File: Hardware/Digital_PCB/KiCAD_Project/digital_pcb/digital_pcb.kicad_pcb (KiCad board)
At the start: 4 copper layers, 75 x 84.8 mm, 85 parts, among them J1 ISP, J2 Board to Board, J3 Conn_01x02, J4 Spare 1, J5 Power, J6 Power Switch, J7 Conn_01x02, Q1 MMBT3904, U1 STM32F103CBTx, U10 TPS793, U2 BNO055, U3 HTU21D, U4 ADS1220, U5 KC2520B-C2, U6 SN74LVC1G17-EP, U7 LT1521-3.3, U8 TEC 2-0921, U9 TPS723, Y1 8MHz, Y2 32.768kHz

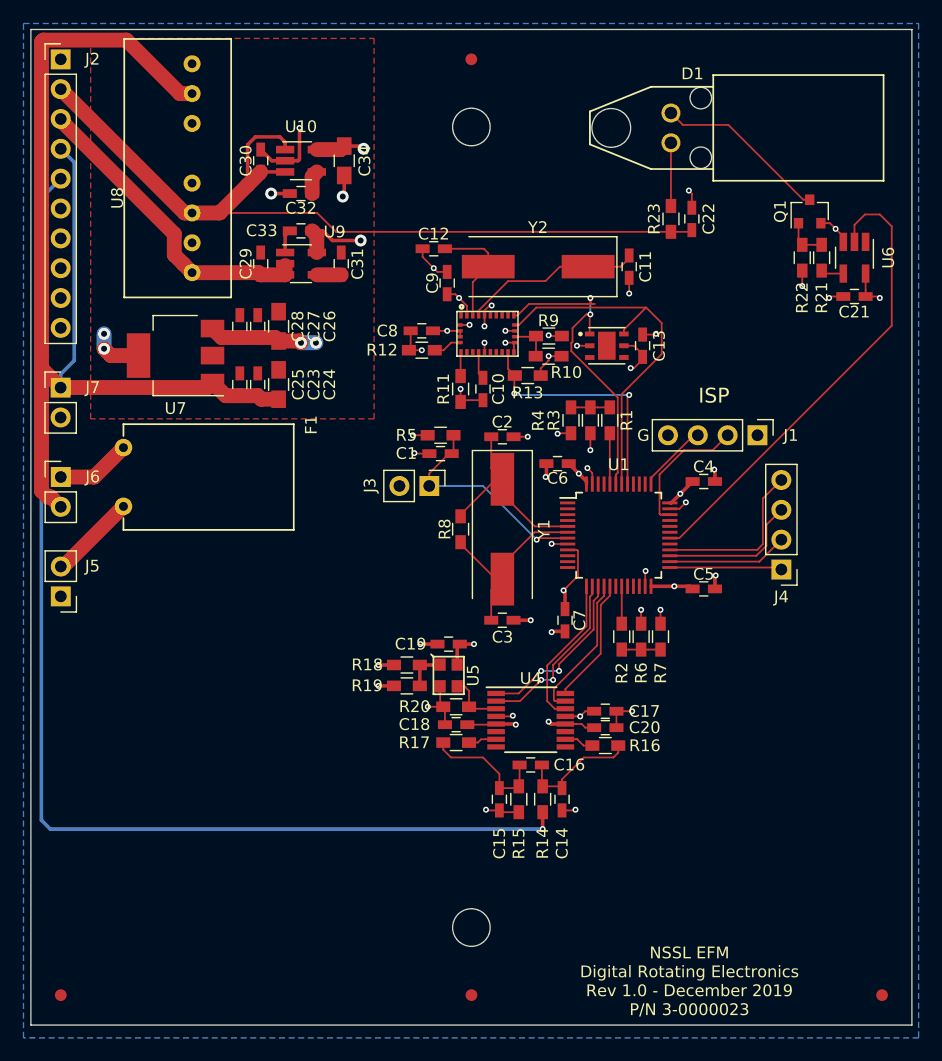
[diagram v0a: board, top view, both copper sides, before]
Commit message: Add pullups and divider for ADC input.
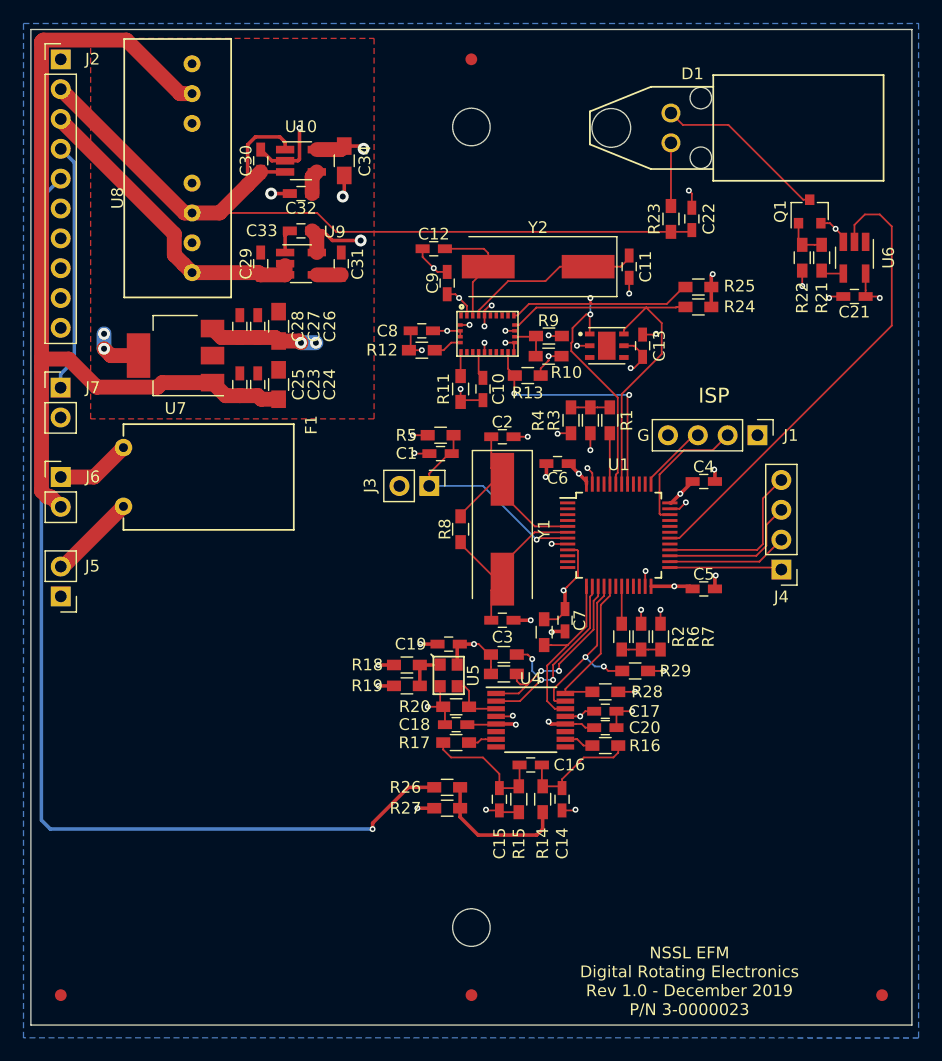
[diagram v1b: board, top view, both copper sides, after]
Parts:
- added R24: 10k, Resistors_SMD:R_0603_HandSoldering, F.Cu at (173.0, 77.5)
- added R25: 10k, Resistors_SMD:R_0603_HandSoldering, F.Cu at (173.0, 75.8)
- added R26: 10k, Resistors_SMD:R_0603_HandSoldering, F.Cu at (151.6, 118.4)
- added R27: 10k, Resistors_SMD:R_0603_HandSoldering, F.Cu at (151.6, 120.1)
- added R28: 10k, Resistors_SMD:R_0603_HandSoldering, F.Cu at (165.1, 110.2)
- added R29: 10k, Resistors_SMD:R_0603_HandSoldering, F.Cu at (167.6, 108.5)
- added R30: 10k, Resistors_SMD:R_0603_HandSoldering, F.Cu at (156.5, 108.7)
- added R31: 10k, Resistors_SMD:R_0603_HandSoldering, F.Cu at (156.5, 107.1)
- added R32: 10k, Resistors_SMD:R_0603_HandSoldering, F.Cu at (159.9, 105.2)
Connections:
- R14 pad 2: AMP_OUT -> Net-(R14-Pad2)
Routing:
- net Net-(R14-Pad2): track 0.00 -> 11.8 mm
- net +3V3: track 51.3 -> 62.6 mm, vias 17 -> 20
- net AMP_OUT: track 99.7 -> 90.8 mm
- net I2C_SDA: track 28.0 -> 36.3 mm
- net SPI1_MISO: track 12.5 -> 16.1 mm, vias 0 -> 2
- net ADC_CS: track 15.0 -> 18.5 mm, vias 2 -> 3
- net I2C_SCL: track 31.8 -> 35.2 mm
- net SPI1_MOSI: track 10.7 -> 13.1 mm
- net ADC_~DRDY: track 13.0 -> 15.0 mm
- net SPI1_SCLK: track 14.7 -> 16.4 mm
- net GND: track 75.8 -> 77.3 mm, vias 42 -> 43
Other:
- board text added: "AMP OUT"

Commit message: Digital PCB Rev 1.0 complete.
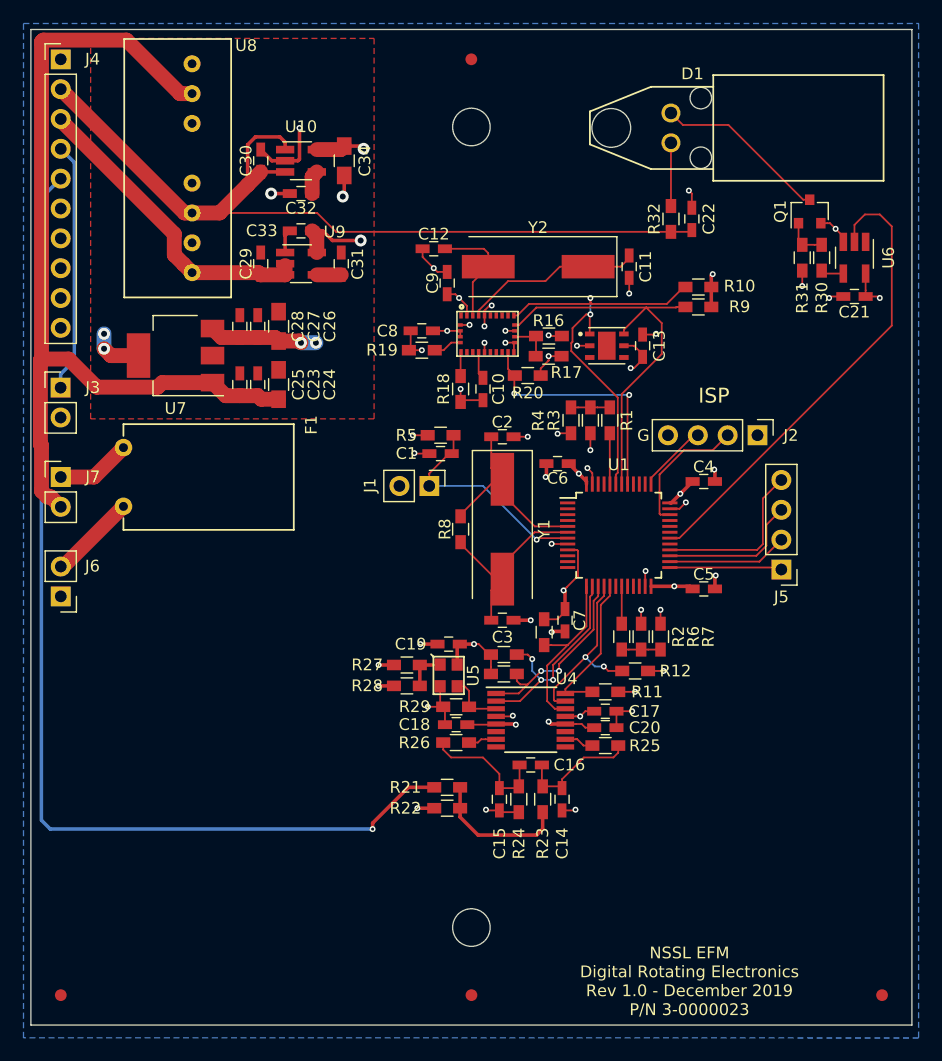
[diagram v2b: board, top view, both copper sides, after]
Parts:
- renumbered J3 to J1, J1 to J2, J7 to J3, J2 to J4, J4 to J5, J5 to J6, J6 to J7, R25 to R10, R28 to R11, R29 to R12, R30 to R13, R31 to R14, R32 to R15, R9 to R16, R10 to R17, R11 to R18, R12 to R19, R13 to R20, R26 to R21, R27 to R22, R14 to R23, R15 to R24, R16 to R25, R17 to R26, R18 to R27, R19 to R28, R20 to R29, R21 to R30, R22 to R31, R23 to R32, R24 to R9

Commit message: Fix flipped fiber transmtter footprint, closes #4.
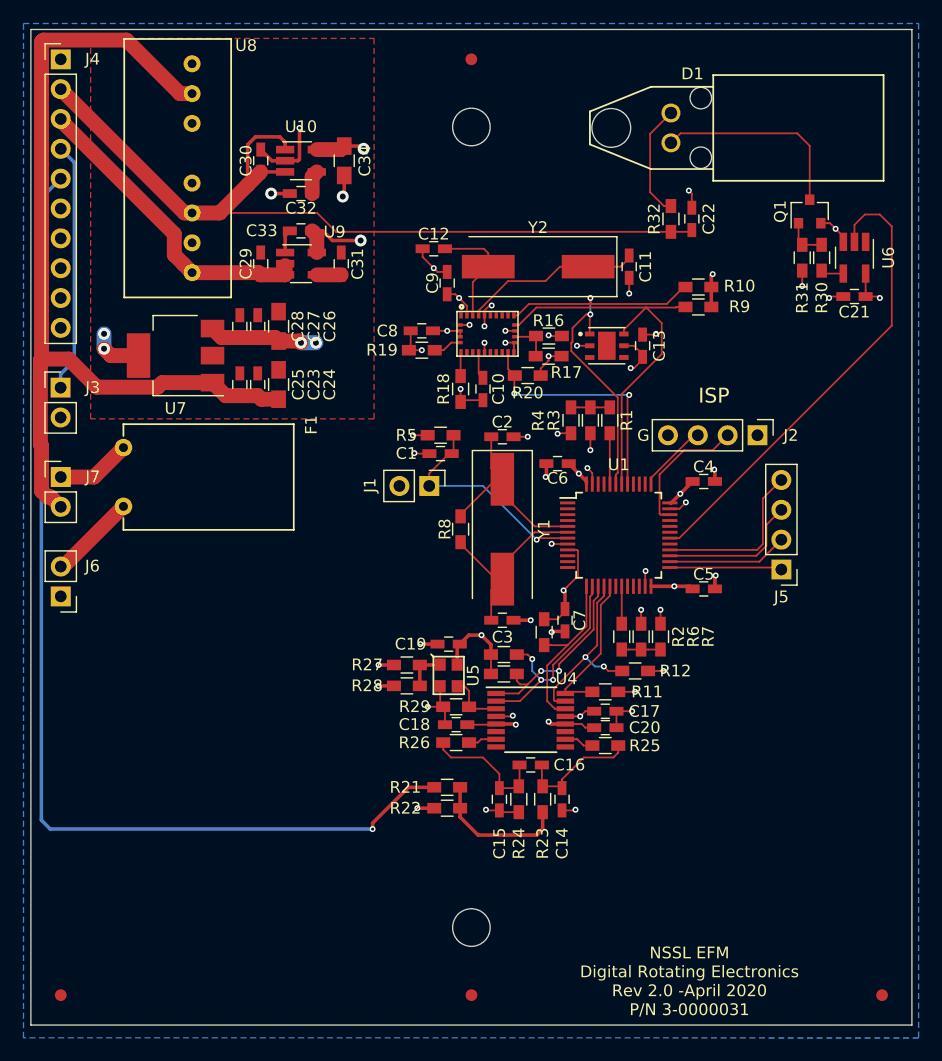
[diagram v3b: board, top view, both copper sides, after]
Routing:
- net Net-(D1-Pad2): track 5.38 -> 9.74 mm
- net Net-(D1-Pad1): track 14.9 -> 17.2 mm
- net +3V3: track 62.6 -> 63.7 mm
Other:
- board text added: "NSSL EFM Digital Rotating Electronics Rev 2.0 -April 2020 P/N 3-0000031"
- board text removed: "NSSL EFM Digital Rotating Electronics Rev 1.0 - December 2019 P/N 3-0000023"

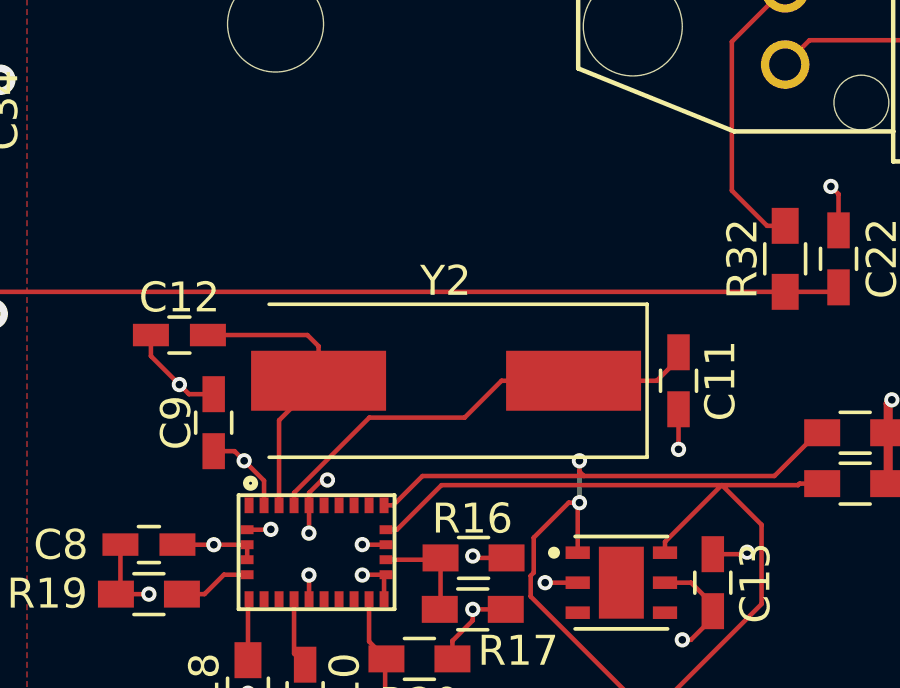
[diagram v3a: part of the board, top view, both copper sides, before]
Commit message: Update IMU crystal footprint to 4-SOJ. closes #5.
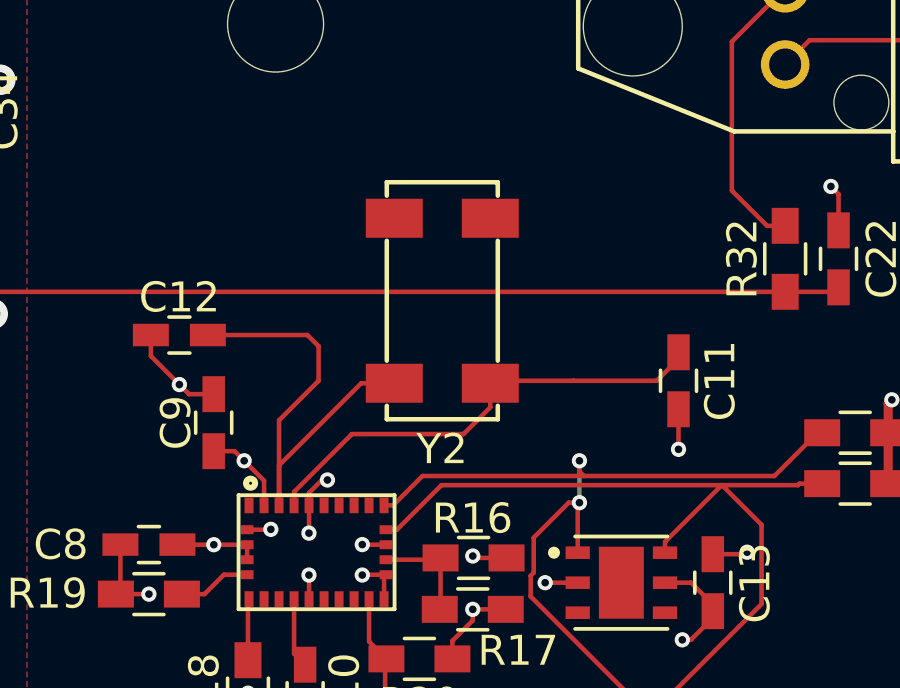
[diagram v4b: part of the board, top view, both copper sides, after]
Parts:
- Y2: footprint Crystals:Crystal_SMD_HC49-SD -> lib_fp:4-SOJ
- moved Y2 2.67 mm to (159.3, 71.4), turned to 90 degrees
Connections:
- J4 pad 10: (no net) -> Net-(J4-Pad10)
- J4 pad 7: (no net) -> Net-(J4-Pad7)
- J4 pad 8: (no net) -> Net-(J4-Pad8)
- J4 pad 9: (no net) -> Net-(J4-Pad9)
- U1 pad 1: (no net) -> Net-(U1-Pad1)
- U1 pad 10: (no net) -> Net-(U1-Pad10)
- U1 pad 11: (no net) -> Net-(U1-Pad11)
- U1 pad 12: (no net) -> Net-(U1-Pad12)
- U1 pad 18: (no net) -> Net-(U1-Pad18)
- U1 pad 2: (no net) -> Net-(U1-Pad2)
- U1 pad 20: (no net) -> Net-(U1-Pad20)
- U1 pad 21: (no net) -> Net-(U1-Pad21)
- U1 pad 22: (no net) -> Net-(U1-Pad22)
- U1 pad 29: (no net) -> Net-(U1-Pad29)
- U1 pad 3: (no net) -> Net-(U1-Pad3)
- U1 pad 31: (no net) -> UART1_RX
- U1 pad 32: (no net) -> Net-(U1-Pad32)
- U1 pad 33: (no net) -> Net-(U1-Pad33)
- U1 pad 38: (no net) -> Net-(U1-Pad38)
- U1 pad 39: (no net) -> Net-(U1-Pad39)
- U1 pad 4: (no net) -> Net-(U1-Pad4)
- U1 pad 40: (no net) -> Net-(U1-Pad40)
- U1 pad 45: (no net) -> Net-(U1-Pad45)
- U1 pad 46: (no net) -> Net-(U1-Pad46)
- U2 pad 1: (no net) -> Net-(U2-Pad1)
- U2 pad 11: (no net) -> Net-(U2-Pad11)
- U2 pad 12: (no net) -> Net-(U2-Pad12)
- U2 pad 13: (no net) -> Net-(U2-Pad13)
- U2 pad 21: (no net) -> Net-(U2-Pad21)
- U2 pad 22: (no net) -> Net-(U2-Pad22)
- U2 pad 23: (no net) -> Net-(U2-Pad23)
- U2 pad 24: (no net) -> Net-(U2-Pad24)
- U2 pad 7: (no net) -> Net-(U2-Pad7)
- U2 pad 8: (no net) -> Net-(U2-Pad8)
- U3 pad 3: (no net) -> Net-(U3-Pad3)
- U3 pad 4: (no net) -> Net-(U3-Pad4)
- U3 pad 7: (no net) -> Net-(U3-Pad7)
- U4 pad 11: (no net) -> Net-(U4-Pad11)
- U4 pad 6: (no net) -> Net-(U4-Pad6)
- U4 pad 8: (no net) -> Net-(U4-Pad8)
- U4 pad 9: (no net) -> Net-(U4-Pad9)
- U6 pad 1: (no net) -> Net-(U6-Pad1)
- U8 pad 3: (no net) -> Net-(U8-Pad3)
- U8 pad 5: (no net) -> Net-(U8-Pad5)
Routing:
- net Net-(C12-Pad2): track 9.69 -> 16.0 mm

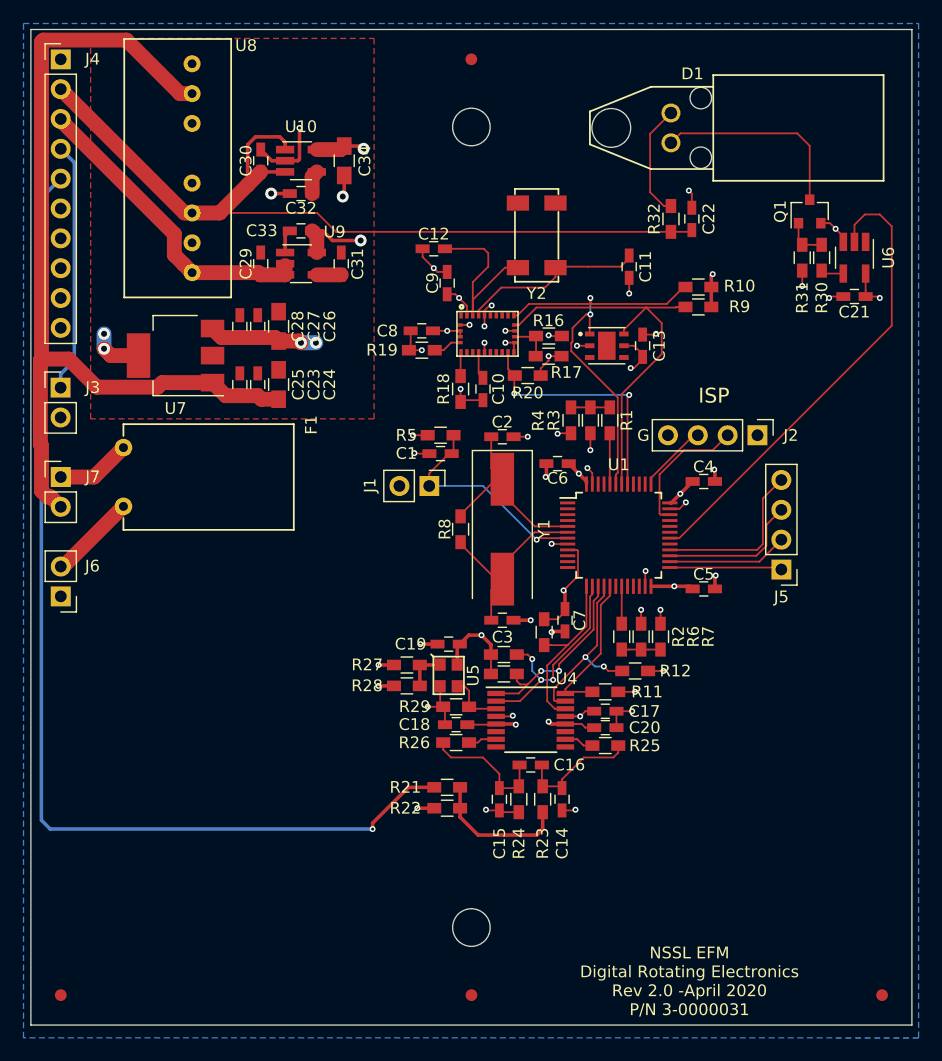
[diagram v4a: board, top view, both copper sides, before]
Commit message: Debounce power switch with load switch and RC timer. Closes #1.
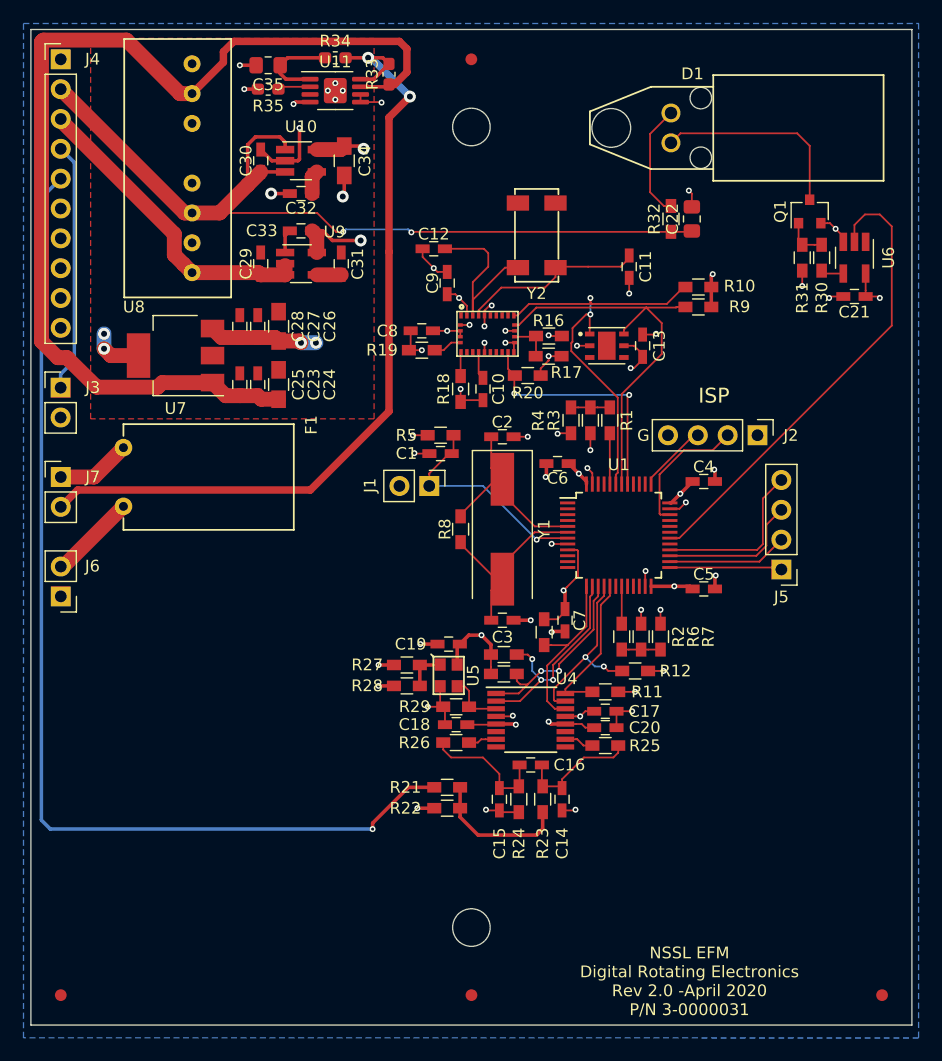
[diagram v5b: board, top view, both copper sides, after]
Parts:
- added C35: 10u, Capacitor_SMD:C_0805_2012Metric_Pad1.15x1.40mm_HandSolder, F.Cu at (136.4, 56.9)
- added R33: 0R0, Resistor_SMD:R_0603_1608Metric_Pad1.05x0.95mm_HandSolder, F.Cu at (146.7, 57.7)
- added R34: 470k, Resistor_SMD:R_0603_1608Metric_Pad1.05x0.95mm_HandSolder, F.Cu at (142.1, 56.3)
- added R35: 10k, Resistor_SMD:R_0603_1608Metric_Pad1.05x0.95mm_HandSolder, F.Cu at (136.4, 58.9)
- added U11: TPS1H000, Package_SO:MSOP-8-1EP_3x3mm_P0.65mm_EP1.95x2.15mm, F.Cu at (142.1, 59.1)
- C22: footprint Capacitors_SMD:C_0603_HandSoldering -> Capacitor_SMD:C_0805_2012Metric_Pad1.15x1.40mm_HandSolder
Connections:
- J7 pad 2: +BATT -> Net-(J7-Pad2)
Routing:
- net Net-(J7-Pad2): track 0.00 -> 70.6 mm, vias 0 -> 2
- net +BATT: track 77.2 -> 90.4 mm
- net GND: track 77.3 -> 86.4 mm, vias 43 -> 51
- net Net-(C35-Pad1): track 0.00 -> 7.52 mm
- net Net-(R35-Pad1): track 0.00 -> 2.77 mm
- net +5V: track 75.9 -> 76.1 mm, vias 0 -> 2
